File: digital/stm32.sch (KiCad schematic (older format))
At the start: 25 parts

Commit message: Finish schematic TODO footprints
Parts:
- removed C?: 4u7, symbol C_Small
- added C207: 4u7, symbol C_Small
- added D201: 3V3, symbol D_Zener
- added R206: 10k, symbol R_Small
- C204: renamed from C?; value 0u1 -> 100n
- TP201, TP202, TP203, TP204, TP205, TP206: renamed from TP?; footprint (none) -> Connectors:PINTST
- gave numbers to parts that had none: 14
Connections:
- net +3V3: now also C207.1
- net GND: now also C207.2, D201.2 (A)
- net at U201.10 (PA0/USART4_TX/ADC_IN0): now also D201.1 (K), R206.2
- net VCO_EN: now reaches U201.25 (PB12/SPI2_NSS)
- net PA_EN: now reaches U201.26 (PB13/SPI2_SCK/I2C2_SCL)
- net LNA1_EN: now reaches U201.27 (PB14/SPI2_MISO/I2C2_SDA)
- net LNA2_EN: now reaches U201.28 (PB15/SPI2_MOSI)
- new net PA_PDET: R206.1
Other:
- moved on the sheet: C208, C209, C210, TP201, TP202, TP203, TP204, TP205, TP206, U201B

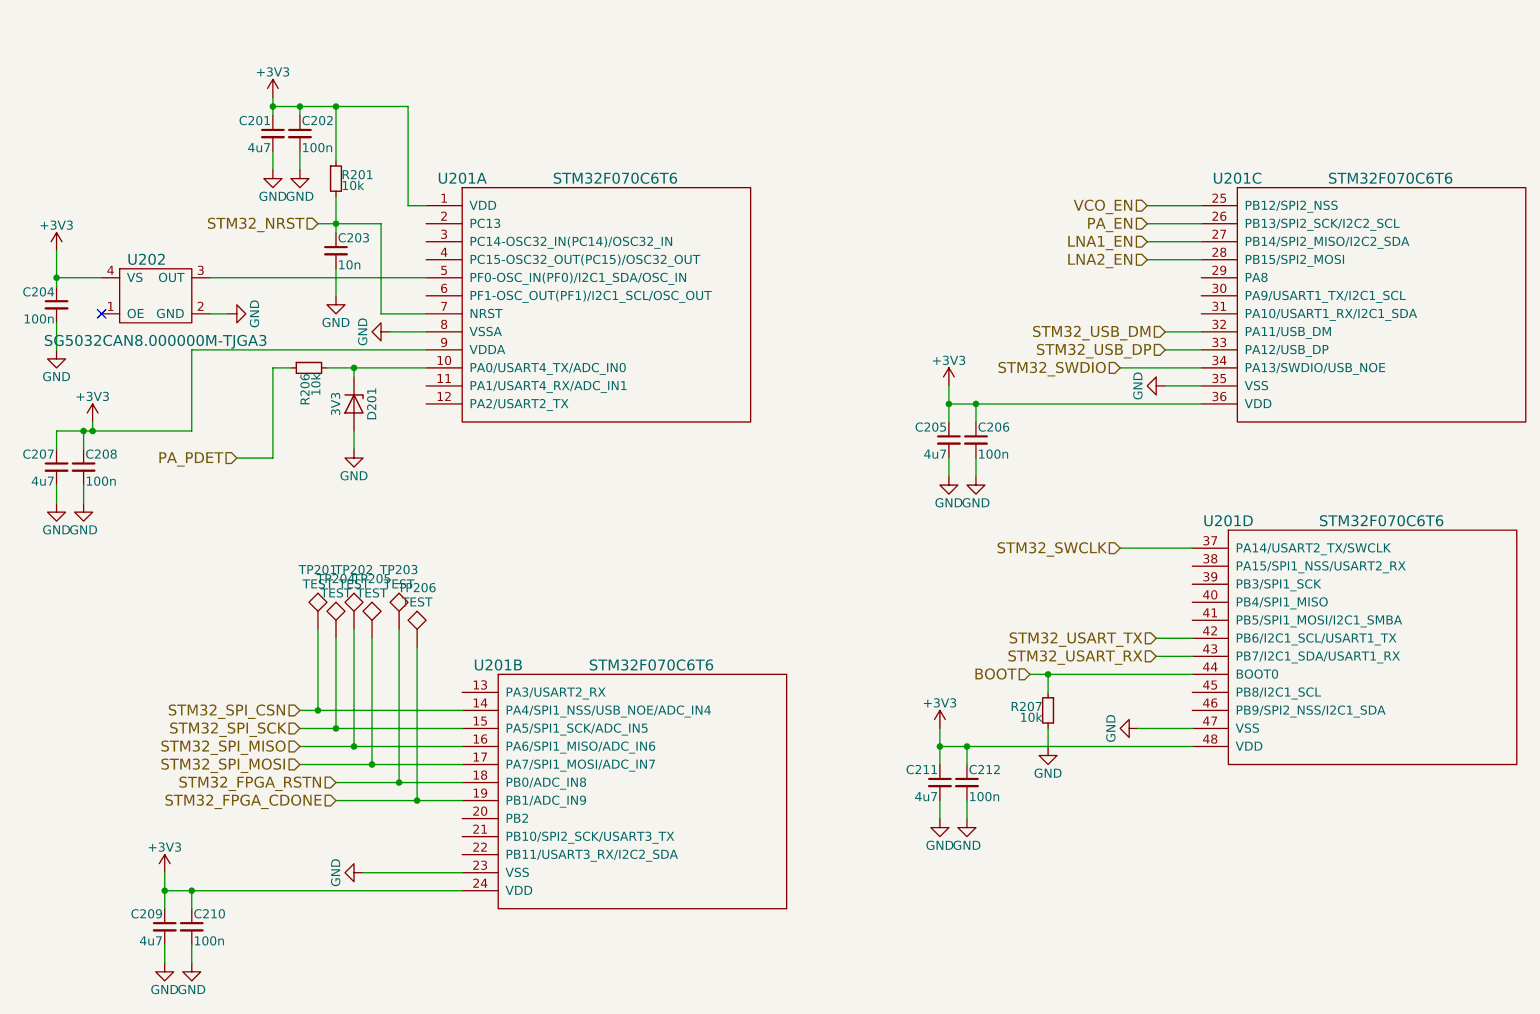
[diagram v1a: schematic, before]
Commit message: Finish schematic and footprinting of digital board
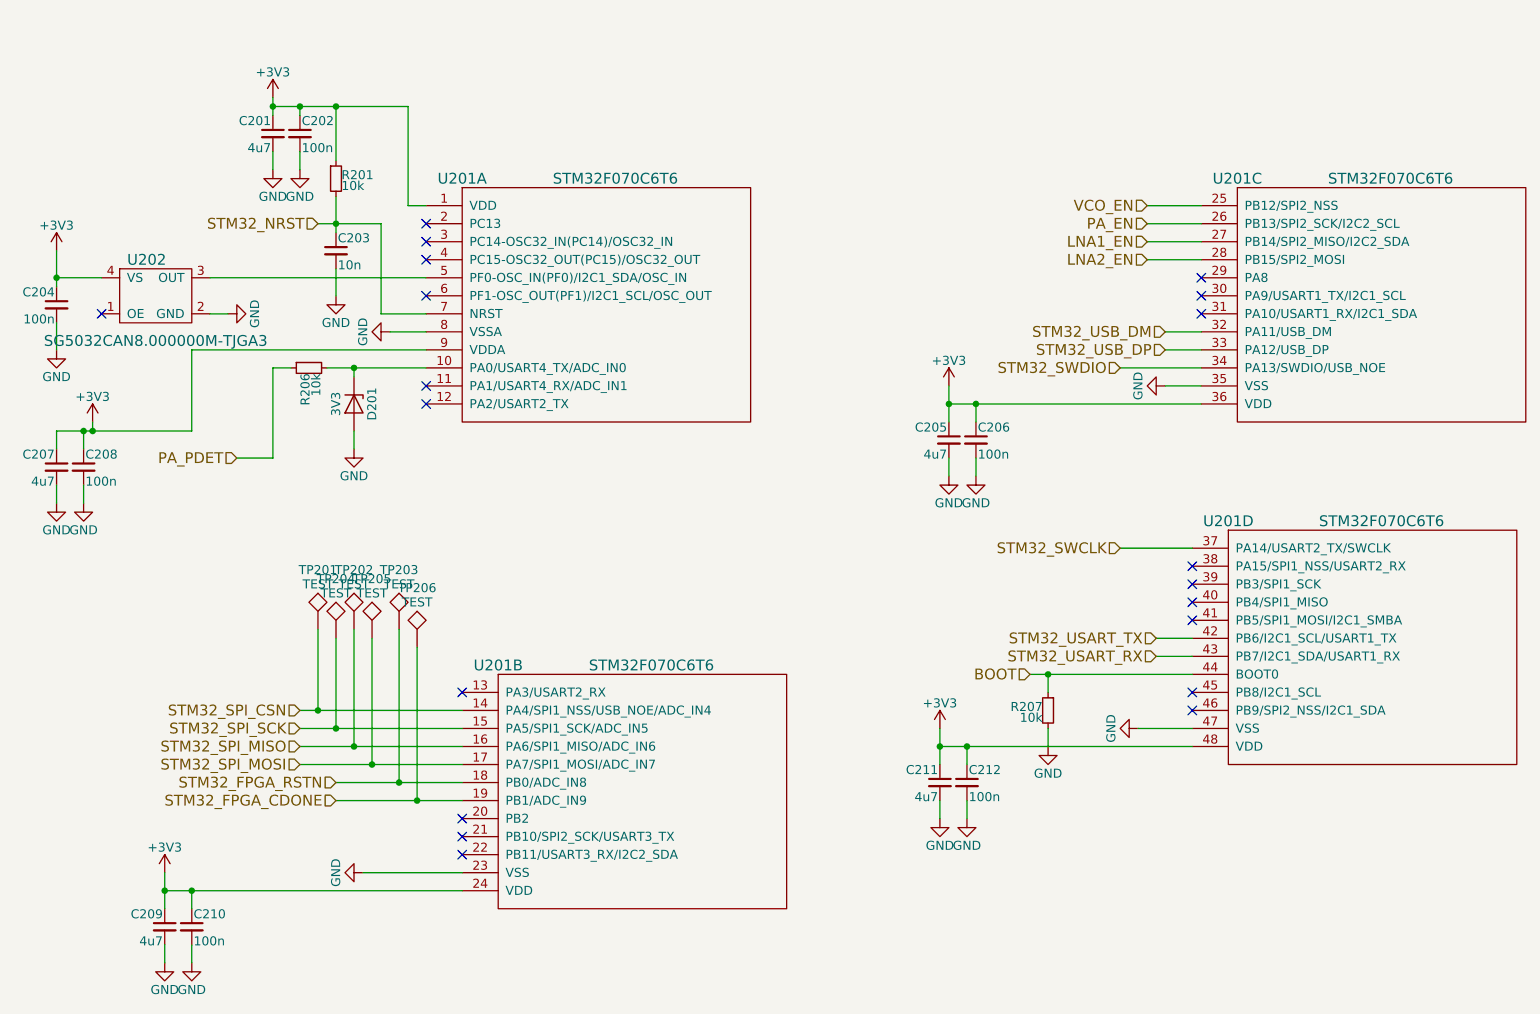
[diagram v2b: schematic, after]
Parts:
- C201, C205, C207, C209, C211: footprint (none) -> Capacitors_SMD:C_1206_HandSoldering
- C202, C204, C206, C208, C210, C212: footprint (none) -> Capacitors_SMD:C_0603_HandSoldering
- C203: footprint (none) -> Capacitors_SMD:C_0402
- D201: footprint (none) -> digital:Diodes_SOD923
- R201, R206, R207: footprint (none) -> Resistors_SMD:R_0603_HandSoldering
- U201: footprint (none) -> digital:ST_LQFP48
- U202: footprint (none) -> Oscillators:Oscillator_SMD_SeikoEpson_SG8002LB-4pin_5.0x3.2mm_HandSoldering
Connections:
- no-connect marks 1 -> 20

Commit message: Line up connectors across both boards, spread out component footprints
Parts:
- TP201, TP202, TP203, TP204, TP205, TP206: footprint Connectors:PINTST -> SMD_Packages:1Pin
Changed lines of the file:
@@
 F 0 "TP201" H 2150 5050 50  0000 C BNN
 F 1 "TEST" H 2150 5000 50  0000 C CNN
-F 2 "Connectors:PINTST" H 2150 4750 50  0001 C CNN
+F 2 "SMD_Packages:1Pin" H 2150 4750 50  0001 C CNN
 F 3 "" H 2150 4750 50  0001 C CNN
 	1    2150 4750
@@
 F 0 "TP204" H 2250 5100 50  0000 C BNN
 F 1 "TEST" H 2250 5050 50  0000 C CNN
-F 2 "Connectors:PINTST" H 2250 4800 50  0001 C CNN
+F 2 "SMD_Packages:1Pin" H 2250 4800 50  0001 C CNN
 F 3 "" H 2250 4800 50  0001 C CNN
 	1    2250 4800
@@
 F 0 "TP202" H 2350 5050 50  0000 C BNN
 F 1 "TEST" H 2350 5000 50  0000 C CNN
-F 2 "Connectors:PINTST" H 2350 4750 50  0001 C CNN
+F 2 "SMD_Packages:1Pin" H 2350 4750 50  0001 C CNN
 F 3 "" H 2350 4750 50  0001 C CNN
 	1    2350 4750
@@
 F 0 "TP205" H 2450 5100 50  0000 C BNN
 F 1 "TEST" H 2450 5050 50  0000 C CNN
-F 2 "Connectors:PINTST" H 2450 4800 50  0001 C CNN
+F 2 "SMD_Packages:1Pin" H 2450 4800 50  0001 C CNN
 F 3 "" H 2450 4800 50  0001 C CNN
 	1    2450 4800
@@
 F 0 "TP203" H 2600 5050 50  0000 C BNN
 F 1 "TEST" H 2600 5000 50  0000 C CNN
-F 2 "Connectors:PINTST" H 2600 4750 50  0001 C CNN
+F 2 "SMD_Packages:1Pin" H 2600 4750 50  0001 C CNN
 F 3 "" H 2600 4750 50  0001 C CNN
 	1    2600 4750
@@
 F 0 "TP206" H 2700 5150 50  0000 C BNN
 F 1 "TEST" H 2700 5100 50  0000 C CNN
-F 2 "Connectors:PINTST" H 2700 4850 50  0001 C CNN
+F 2 "SMD_Packages:1Pin" H 2700 4850 50  0001 C CNN
 F 3 "" H 2700 4850 50  0001 C CNN
 	1    2700 4850

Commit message: Finish digital layout
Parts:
- removed TP206: TEST, SMD_Packages:1Pin, symbol TEST
- TP201, TP202, TP203, TP204, TP205: footprint SMD_Packages:1Pin -> Measurement_Points:Measurement_Point_Round-SMD-Pad_Small
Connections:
- net LNA1_EN: now also U201.3 (PC14-OSC32_IN(PC14)/OSC32_IN); no longer U201.27 (PB14/SPI2_MISO/I2C2_SDA)
- net LNA2_EN: now also U201.2 (PC13); no longer U201.28 (PB15/SPI2_MOSI)
- net PA_EN: now also U201.13 (PA3/USART2_RX); no longer U201.26 (PB13/SPI2_SCK/I2C2_SCL)
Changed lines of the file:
@@
 LIBS:tlv74125pdbvr
 LIBS:opa2376qdgkrq1
+LIBS:tlv74312pdbvr
 LIBS:digital-cache
 EELAYER 25 0
@@
 F 0 "TP201" H 2150 5050 50  0000 C BNN
 F 1 "TEST" H 2150 5000 50  0000 C CNN
-F 2 "SMD_Packages:1Pin" H 2150 4750 50  0001 C CNN
+F 2 "Measurement_Points:Measurement_Point_Round-SMD-Pad_Small" H 2150 4750 50  0001 C CNN
 F 3 "" H 2150 4750 50  0001 C CNN
 	1    2150 4750
@@
 F 0 "TP204" H 2250 5100 50  0000 C BNN
 F 1 "TEST" H 2250 5050 50  0000 C CNN
-F 2 "SMD_Packages:1Pin" H 2250 4800 50  0001 C CNN
+F 2 "Measurement_Points:Measurement_Point_Round-SMD-Pad_Small" H 2250 4800 50  0001 C CNN
 F 3 "" H 2250 4800 50  0001 C CNN
 	1    2250 4800
@@
 F 0 "TP202" H 2350 5050 50  0000 C BNN
 F 1 "TEST" H 2350 5000 50  0000 C CNN
-F 2 "SMD_Packages:1Pin" H 2350 4750 50  0001 C CNN
+F 2 "Measurement_Points:Measurement_Point_Round-SMD-Pad_Small" H 2350 4750 50  0001 C CNN
 F 3 "" H 2350 4750 50  0001 C CNN
 	1    2350 4750
@@
 F 0 "TP205" H 2450 5100 50  0000 C BNN
 F 1 "TEST" H 2450 5050 50  0000 C CNN
-F 2 "SMD_Packages:1Pin" H 2450 4800 50  0001 C CNN
+F 2 "Measurement_Points:Measurement_Point_Round-SMD-Pad_Small" H 2450 4800 50  0001 C CNN
 F 3 "" H 2450 4800 50  0001 C CNN
 	1    2450 4800
@@
 F 0 "TP203" H 2600 5050 50  0000 C BNN
 F 1 "TEST" H 2600 5000 50  0000 C CNN
-F 2 "SMD_Packages:1Pin" H 2600 4750 50  0001 C CNN
+F 2 "Measurement_Points:Measurement_Point_Round-SMD-Pad_Small" H 2600 4750 50  0001 C CNN
 F 3 "" H 2600 4750 50  0001 C CNN
 	1    2600 4750
@@
 Text HLabel 2250 5700 0    60   Input ~ 0
 STM32_FPGA_CDONE
-$Comp
-L TEST TP206
-U 1 1 5AD3F915
-P 2700 4850
-F 0 "TP206" H 2700 5150 50  0000 C BNN
-F 1 "TEST" H 2700 5100 50  0000 C CNN
-F 2 "SMD_Packages:1Pin" H 2700 4850 50  0001 C CNN
-F 3 "" H 2700 4850 50  0001 C CNN
-	1    2700 4850
-	1    0    0    -1
-$EndComp
 Text HLabel 6750 2400 0    60   Input ~ 0
 VCO_EN
-Text HLabel 6750 2500 0    60   Input ~ 0
+Text HLabel 1450 5100 0    60   Input ~ 0
 PA_EN
-Text HLabel 6750 2600 0    60   Input ~ 0
+Text HLabel 1350 1500 0    60   Input ~ 0
 LNA1_EN
-Text HLabel 6750 2700 0    60   Input ~ 0
+Text HLabel 1350 1400 0    60   Input ~ 0
 LNA2_EN
 Text HLabel 1700 3800 0    60   Input ~ 0
@@
 	2250 5700 2950 5700
 Wire Wire Line
-	2700 4850 2700 5700
-Connection ~ 2700 5700
-Wire Wire Line
 	1700 3800 1900 3800
 Wire Wire Line
 	2200 3300 2750 3300
 Wire Wire Line
-	6750 2500 7050 2500
+	1450 5100 2950 5100
 Wire Wire Line
 	6750 2400 7050 2400
 Wire Wire Line
-	6750 2600 7050 2600
-Wire Wire Line
-	6750 2700 7050 2700
+	1350 1400 2600 1400
+Wire Wire Line
+	1350 1500 2550 1500
 Wire Wire Line
 	1450 3650 1450 3200
@@
 Wire Wire Line
 	2350 3650 2350 3750
-NoConn ~ 2750 2500
-NoConn ~ 2750 2600
 NoConn ~ 2750 2700
 NoConn ~ 2750 2900
 NoConn ~ 2750 3400
 NoConn ~ 2750 3500
-NoConn ~ 2950 5100
+NoConn ~ 7050 2500
 NoConn ~ 2950 5800
 NoConn ~ 2950 5900
@@
 NoConn ~ 7000 5100
 NoConn ~ 7000 5200
+Wire Wire Line
+	2600 1400 2600 2500
+Wire Wire Line
+	2600 2500 2750 2500
+Wire Wire Line
+	2550 1500 2550 2600
+Wire Wire Line
+	2550 2600 2750 2600
+NoConn ~ 7050 2600
+NoConn ~ 7050 2700
 $EndSCHEMATC
